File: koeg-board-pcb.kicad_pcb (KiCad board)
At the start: 2 copper layers, 229.8 x 84.3 mm, 218 parts, among them J1 Conn_01x02, J2 SWD_Connector, J3 USB_C_Receptacle_USB2.0_14P, J4 Conn_01x02, J5 SWD_Connector, J6 USB_C_Receptacle_USB2.0_14P, Q1 BSS138, Q2 BSS138, SW1 Reset Button, SW10 SW_Push, SW11 SW_Push, SW12 SW_Push, SW13 SW_Push, SW14 SW_Push, SW15 SW_Push, SW16 SW_Push, SW17 SW_Push, SW18 SW_Push, SW19 SW_Push, SW2 SW_On_Off, SW20 SW_Push, SW21 SW_Push, SW22 SW_Push, SW23 SW_Push, SW24 Reset Button, SW25 SW_On_Off, SW26 SW_Push, SW27 SW_Push, SW28 SW_Push, SW29 SW_Push, SW3 SW_Push, SW30 SW_Push, SW31 SW_Push, SW32 SW_Push, SW33 SW_Push, SW34 SW_Push, SW35 SW_Push, SW36 SW_Push, SW37 SW_Push, SW38 SW_Push, SW39 SW_Push, SW4 SW_Push, SW40 SW_Push, SW41 SW_Push, SW42 SW_Push, SW43 SW_Push, SW44 SW_Push, SW45 SW_Push, SW46 SW_Push, SW5 SW_Push, SW6 SW_Push, SW7 SW_Push, SW8 SW_Push, SW9 SW_Push, U1 nRF52840, U2 USBLC6-2SC6, U3 AMS1117-5.0, U4 nRF52840, U5 USBLC6-2SC6, U6 AMS1117-5.0, Y1 JYJE 2TJ432000NYFBC, Y2 JYJE 2TJ432000NYFBC

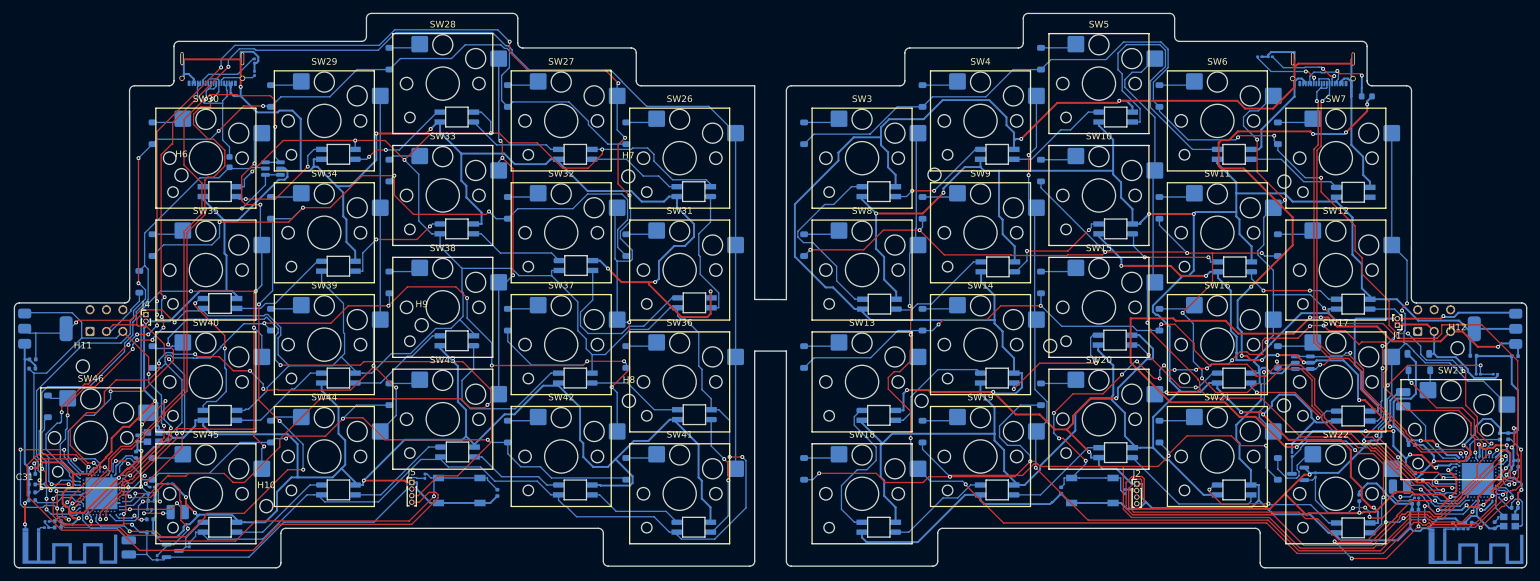
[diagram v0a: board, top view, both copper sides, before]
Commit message: added propper brake offs
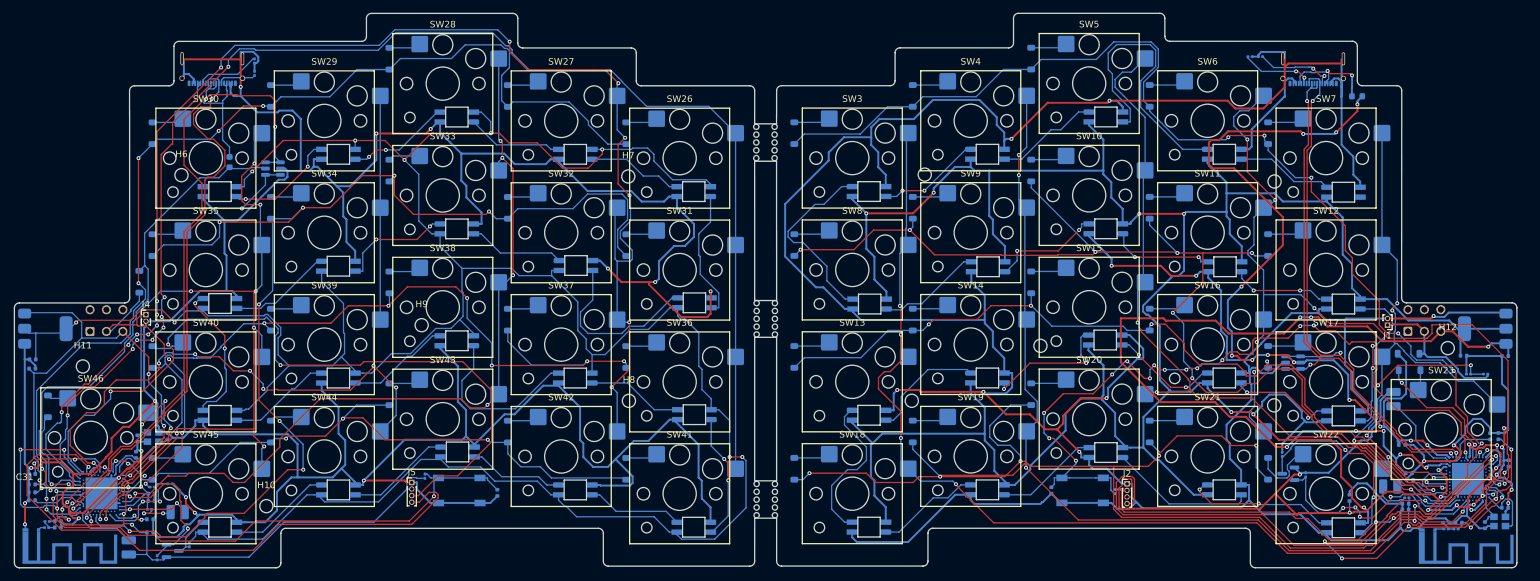
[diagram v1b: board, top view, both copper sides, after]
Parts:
- added P2: Breakoff, jiran-ble-lite:Panel_2x5, F.Cu at (145.4, 100.6)
- added P2: Breakoff, jiran-ble-lite:Panel_2x5, F.Cu at (145.4, 73.8)
- added P2: Breakoff, jiran-ble-lite:Panel_2x5, F.Cu at (145.4, 128.1)
- moved C11 1.49 mm to (257.8, 129.3)
- moved C13 1.49 mm to (250.7, 131.6)
- moved C7 1.49 mm to (242.6, 129.6)
- moved AE1 1.49 mm to (246.4, 133.0)
- moved C1 1.49 mm to (242.1, 119.8)
- moved C10 1.49 mm to (234.1, 127.8)
- moved C15 1.49 mm to (257.8, 106.3)
- moved C16 1.49 mm to (251.5, 106.2)
- moved C2 1.49 mm to (188.8, 126.7)
- moved C4 1.49 mm to (243.3, 125.1)
- moved C5 1.49 mm to (256.8, 118.4)
- moved C6 1.49 mm to (258.3, 122.6)
- moved C8 1.49 mm to (242.6, 128.7)
- moved C9 1.49 mm to (255.5, 118.5)
- moved D1 1.49 mm to (243.1, 105.9)
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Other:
- board size 229.8 x 84.3 mm -> 228.3 x 84.3 mm
